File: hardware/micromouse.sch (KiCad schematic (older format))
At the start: 45 parts, among them U1 STM32F446RE_LQFP64

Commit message: updated PCB design
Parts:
- removed LED_RED4: Led_Small, symbol Led_Small
- removed R12: 1k, symbol R_Small
- removed R_RESET?: 47k, symbol R_Small
- added CN1, CN2: 5_PIN_HEADER, Pin_Headers:Pin_Header_Straight_1x05, symbol 5_PIN_HEADER
- added C_M1: 220uF, Capacitors_Tantalum_SMD:TantalC_SizeD_EIA-7343_HandSoldering, symbol CP_Small
- added C_V1, C_V2, C_V3, C_V4, C_V5, C_V6: 0.1uF, Capacitors_SMD:C_0603_HandSoldering, symbol C_Small
- added C_VCAP1, C_VCAP2: 2.2uF, Capacitors_SMD:C_1206_HandSoldering, symbol C_Small
- added L_BEAD1: 10uH, Resistors_SMD:R_0603_HandSoldering, symbol BEAD
- added R_BOOT1, R_VOL2: 10k, Resistors_SMD:R_0603_HandSoldering, symbol R_Small
- added R_VOL1: 20k, Resistors_SMD:R_0603_HandSoldering, symbol R_Small
- CNR1: renamed from CNR; footprint (none) -> Capacitors_SMD:C_0603_HandSoldering
- C_3.3V1: renamed from C_3.3V?; footprint (none) -> Capacitors_SMD:C_1206_HandSoldering
- C_3.3V2: renamed from C_3.3V?; footprint (none) -> Capacitors_SMD:C_0603_HandSoldering
- C_5V1: renamed from C_5V?; footprint (none) -> Capacitors_SMD:C_1210_HandSoldering
- C_5V2: renamed from C_5V?; footprint (none) -> Capacitors_SMD:C_0603_HandSoldering
- C_RESET1: renamed from C_RESET?; footprint (none) -> Capacitors_SMD:C_0603_HandSoldering
- C_VBAT1: renamed from C_VBAT?; footprint (none) -> Capacitors_SMD:C_1210_HandSoldering
- C_VBAT2: renamed from C_VBAT?; footprint (none) -> Capacitors_SMD:C_0603_HandSoldering
- D_PWR1: renamed from D_PWR?; footprint (none) -> LEDs:LED_0603
- LED_BLUE1, LED_BLUE2, LED_BLUE3, LED_BLUE4, LED_GREEN1, LED_GREEN2, LED_GREEN3, LED_GREEN4, LED_RED1, LED_RED2, LED_RED3: footprint (none) -> LEDs:LED_0603
- M2: renamed from M?; footprint JST_CONNECTOR_FEMALE.-THROUGH -> pcb1:JST_CONNECTOR_FEMALE.-THROUGH-HOLE_JST_CONNECTOR_FEMALE
- M3: renamed from M?; footprint 2.54MM-SLIDE-SWITCH_TS02_SWITCH -> pcb1:2.54MM-SLIDE-SWITCH_TS02_SWITCH
- R1, R10, R11, R2, R3, R4, R5, R6, R7, R8, R9: footprint (none) -> Resistors_SMD:R_0603_HandSoldering
- R_PB1, R_PB2: renamed from R_PB?; footprint (none) -> Resistors_SMD:R_0603_HandSoldering
- R_PWR1: renamed from R_PWR?; footprint (none) -> Resistors_SMD:R_0603_HandSoldering
- SW1, SW2, SW3: renamed from SW?; footprint (none) -> Buttons_Switches_SMD:SW_SPST_PTS645
- U1: footprint STM32F446RE_LQFP64 -> footprints_micromouse:STM32F446_LQFP64
- U11: renamed from U?; footprint (none) -> footprints_micromouse:TPS76850_SOIC-8
- U12: renamed from U?; footprint (none) -> footprints_micromouse:TPS73633_SOT-23
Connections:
- net LED11 is gone; now on net LED10: U1.PC7
- net +3V3: now also U1.VBAT, U1.VDD_ (VDD_3), CN2.1, C_V2.2, C_V3.1, C_V4.2, C_V5.2, C_V6.2, L_BEAD1.1
- net +BATT: now also C_M1.1, R_VOL1.1; no longer CNR1.2, C_3.3V1.2, C_3.3V2.2, C_5V1.2, C_5V2.2, C_RESET1.2, C_VBAT1.2, C_VBAT2.2, D_PWR1.1 (K), LED_BLUE1.1 (K), LED_BLUE2.1 (K), LED_BLUE3.1 (K), LED_BLUE4.1 (K), LED_GREEN1.1 (K), LED_GREEN2.1 (K), LED_GREEN3.1 (K), LED_GREEN4.1 (K), LED_RED1.1 (K), LED_RED2.1 (K), LED_RED3.1 (K), M2.-, R_PB1.2, R_PB2.2, SW3.2, U11.1 (GND), U11.2 (~EN), U12.2 (GND)
- net LED10: no longer U1.PC6
- net LED9: now also U1.PC6; no longer U1.PB1
- net RESET: now also U1.NRST, CN2.5
- net USART_RX: now also CN1.4
- net USART_TX: now also CN1.5
- net at U1.BOOT (BOOT0): now also R_BOOT1.2
- net SWDIO: now reaches U1.PA13
- net SWDIO: now also CN2.4
- net SWCLK: now reaches U1.PA14
- net SWCLK: now also CN2.2
- net at U1.PB11 (VCAP_1): now also C_VCAP1.1
- net GND: now reaches U1.VCAP (VSS)
- net GND: now also CNR1.2, C_3.3V1.2, C_3.3V2.2, C_5V1.2, C_5V2.2, C_RESET1.2, C_VBAT1.2, C_VBAT2.2, D_PWR1.1 (K), LED_BLUE1.1 (K), LED_BLUE2.1 (K), LED_BLUE3.1 (K), LED_BLUE4.1 (K), LED_GREEN1.1 (K), LED_GREEN2.1 (K), LED_GREEN3.1 (K), LED_GREEN4.1 (K), LED_RED1.1 (K), LED_RED2.1 (K), LED_RED3.1 (K), M2.-, R_PB1.2, R_PB2.2, SW3.2, U1.VSSA, U1.VSS_ (VSS_1), U11.1 (GND), U11.2 (~EN), U12.2 (GND), CN1.1, CN2.3, C_M1.2, C_V1.2, C_V2.1, C_V3.2, C_V4.1, C_V5.1, C_V6.1, C_VCAP1.2, C_VCAP2.1, C_VCAP2.2, R_BOOT1.1, R_VOL2.2
- net +3.3VADC: now reaches U1.VDDA
- net +3.3VADC: now also C_V1.1, L_BEAD1.2
- new net VOL_METER: R_VOL1.2, R_VOL2.1, U1.PB1
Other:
- note added: "NRST Pin has \ninternal permanent\npull-up resistor \nso pull-up is \nnot needed"
- moved on the sheet: CNR1, C_3.3V1, C_3.3V2, C_5V1, C_5V2, C_RESET1, C_VBAT1, C_VBAT2, D_PWR1, R_PWR1, SW3, U11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

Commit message: PCB updated
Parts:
- removed LED_BLUE1, LED_BLUE2, LED_BLUE3, LED_BLUE4, LED_GREEN1, LED_GREEN3, LED_GREEN4, LED_RED2, LED_RED3: Led_Small, LEDs:LED_0603, symbol Led_Small
- removed R1, R10, R11, R2, R3, R6, R7, R8, R9: 1k, Resistors_SMD:R_0603_HandSoldering, symbol R_Small
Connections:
- net labels removed: LED0, LED1, LED10, LED2, LED5, LED6, LED7, LED8, LED9
- wire segments 270 -> 243

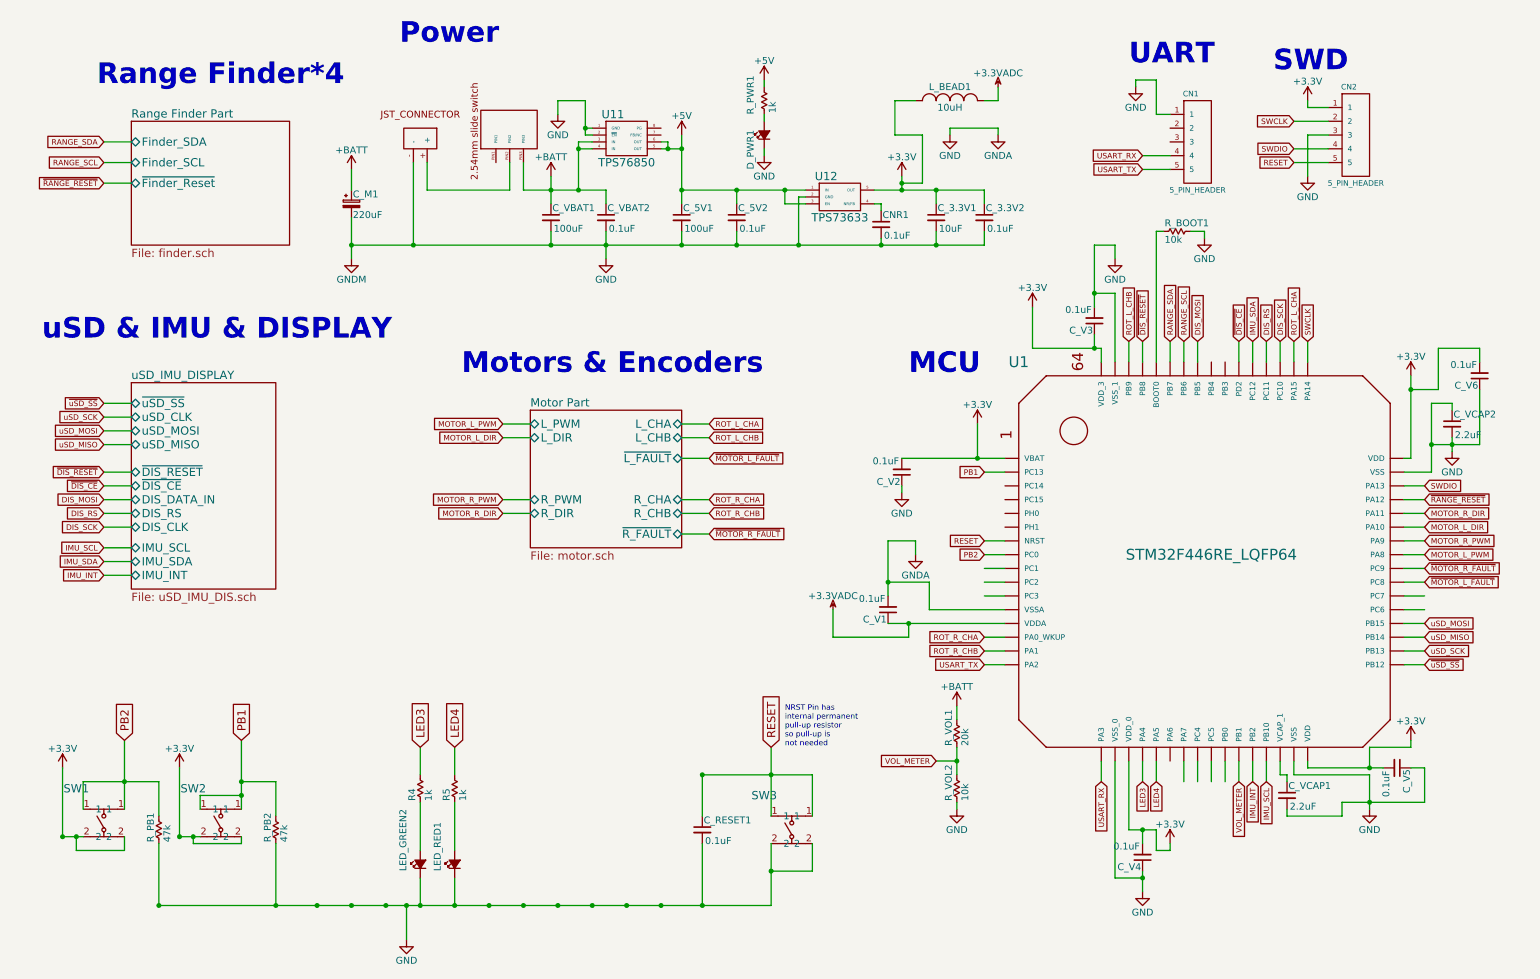
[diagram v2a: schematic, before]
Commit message: PCB board- needs to check the motor driver
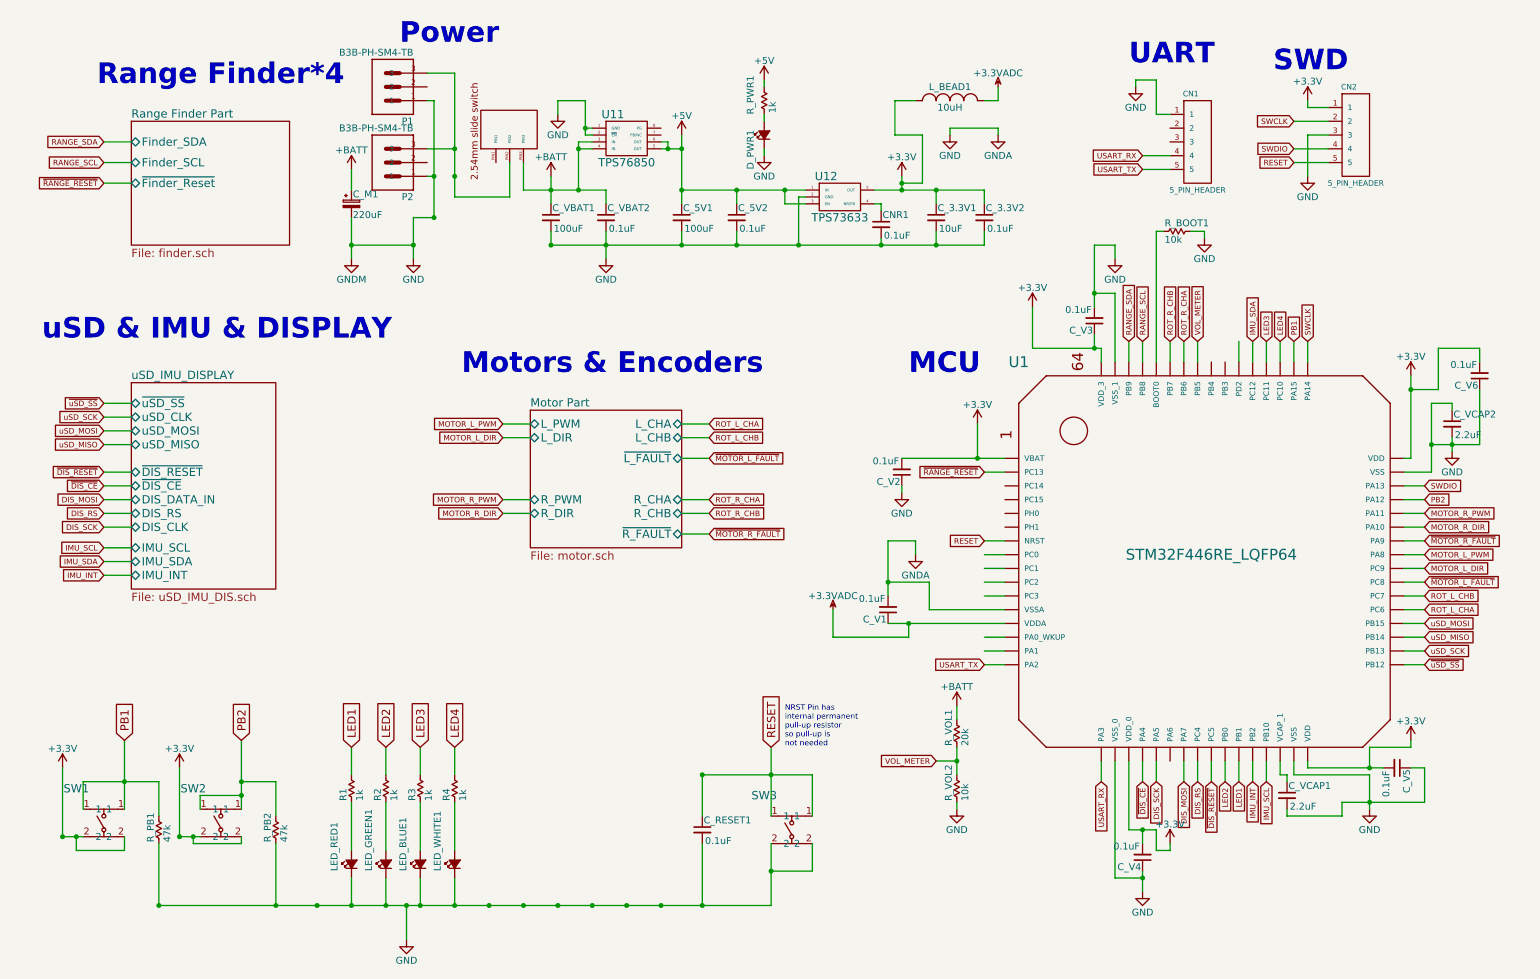
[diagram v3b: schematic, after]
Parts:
- removed M2: JST_CONNECTOR_FEMALE.-THROUGH, pcb1:JST_CONNECTOR_FEMALE.-THROUGH-HOLE_JST_CONNECTOR_FEMALE, symbol JST_CONNECTOR_FEMALE.-THROUGH
- added LED_GREEN1, LED_RED1: Led_Small, LEDs:LED_0603, symbol Led_Small
- added P1, P2: B3B-PH-SM4-TB, footprints_micromouse:JST_B3B-PH_HEADER, symbol B3B-PH-SM4-TB
- added R1, R2: 1k, Resistors_SMD:R_0603, symbol R_Small
- CNR1, C_3.3V2, C_5V2, C_RESET1, C_V1, C_V2, C_V3, C_V4, C_V5, C_V6, C_VBAT2: footprint Capacitors_SMD:C_0603_HandSoldering -> Capacitors_SMD:C_0603
- C_3.3V1, C_VCAP1, C_VCAP2: footprint Capacitors_SMD:C_1206_HandSoldering -> Capacitors_SMD:C_1206
- C_5V1, C_VBAT1: footprint Capacitors_SMD:C_1210_HandSoldering -> Capacitors_SMD:C_1210
- L_BEAD1, R_BOOT1, R_PB1, R_PB2, R_PWR1, R_VOL1, R_VOL2: footprint Resistors_SMD:R_0603_HandSoldering -> Resistors_SMD:R_0603
- R3: renamed from R4; footprint Resistors_SMD:R_0603_HandSoldering -> Resistors_SMD:R_0603
- R4: renamed from R5; footprint Resistors_SMD:R_0603_HandSoldering -> Resistors_SMD:R_0603
- renumbered LED_GREEN2 to LED_BLUE1, LED_RED1 to LED_WHITE1
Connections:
- net labels added: LED1, LED2
- wire segments 243 -> 256

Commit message: PCB Completed
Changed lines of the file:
@@
 	3400 1000 3600 1000
 Wire Wire Line
-	3600 1900 4000 1900
+	4000 1900 3600 1900
 Connection ~ 3600 1750
 Wire Wire Line
@@
 	3400 1750 3450 1750
 Wire Wire Line
-	3600 1000 3600 1900
+	3600 1900 3600 1000
 Wire Wire Line
 	3400 1200 3450 1200
